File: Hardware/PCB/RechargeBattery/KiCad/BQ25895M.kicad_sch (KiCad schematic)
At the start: 19 parts, among them IC1 BQ25895MRTWT, J1 USB_C_Receptacle_USB2.0_16P

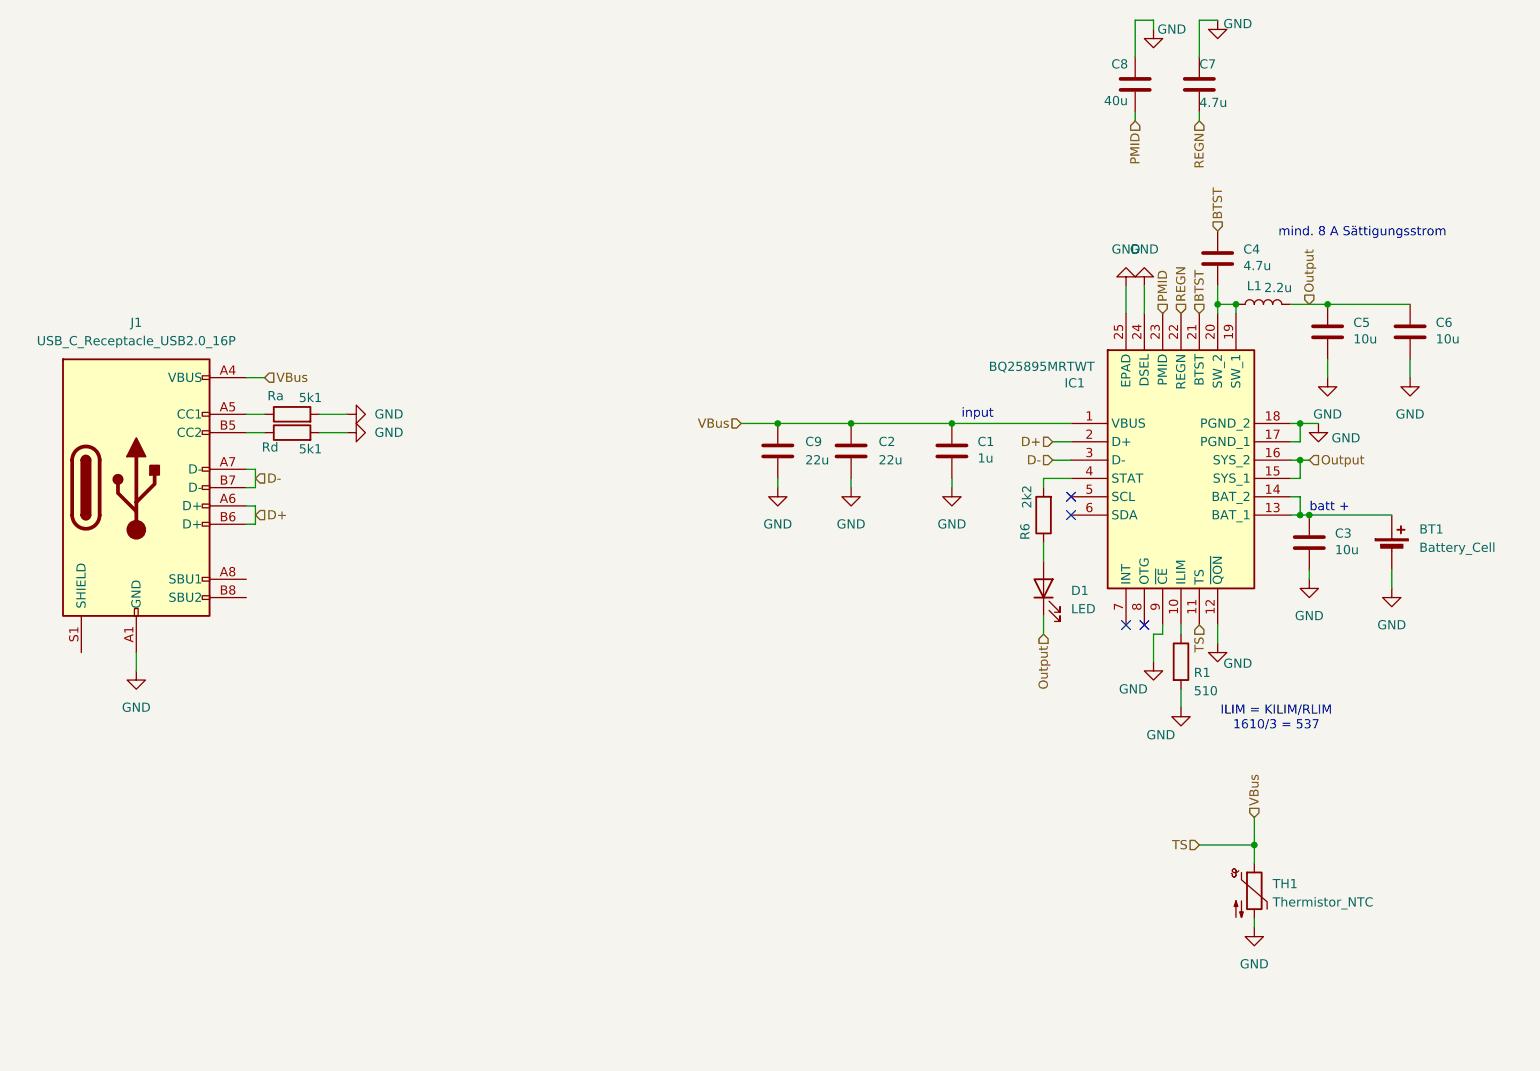
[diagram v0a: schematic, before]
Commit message: rechargeBatterie schematic finsished
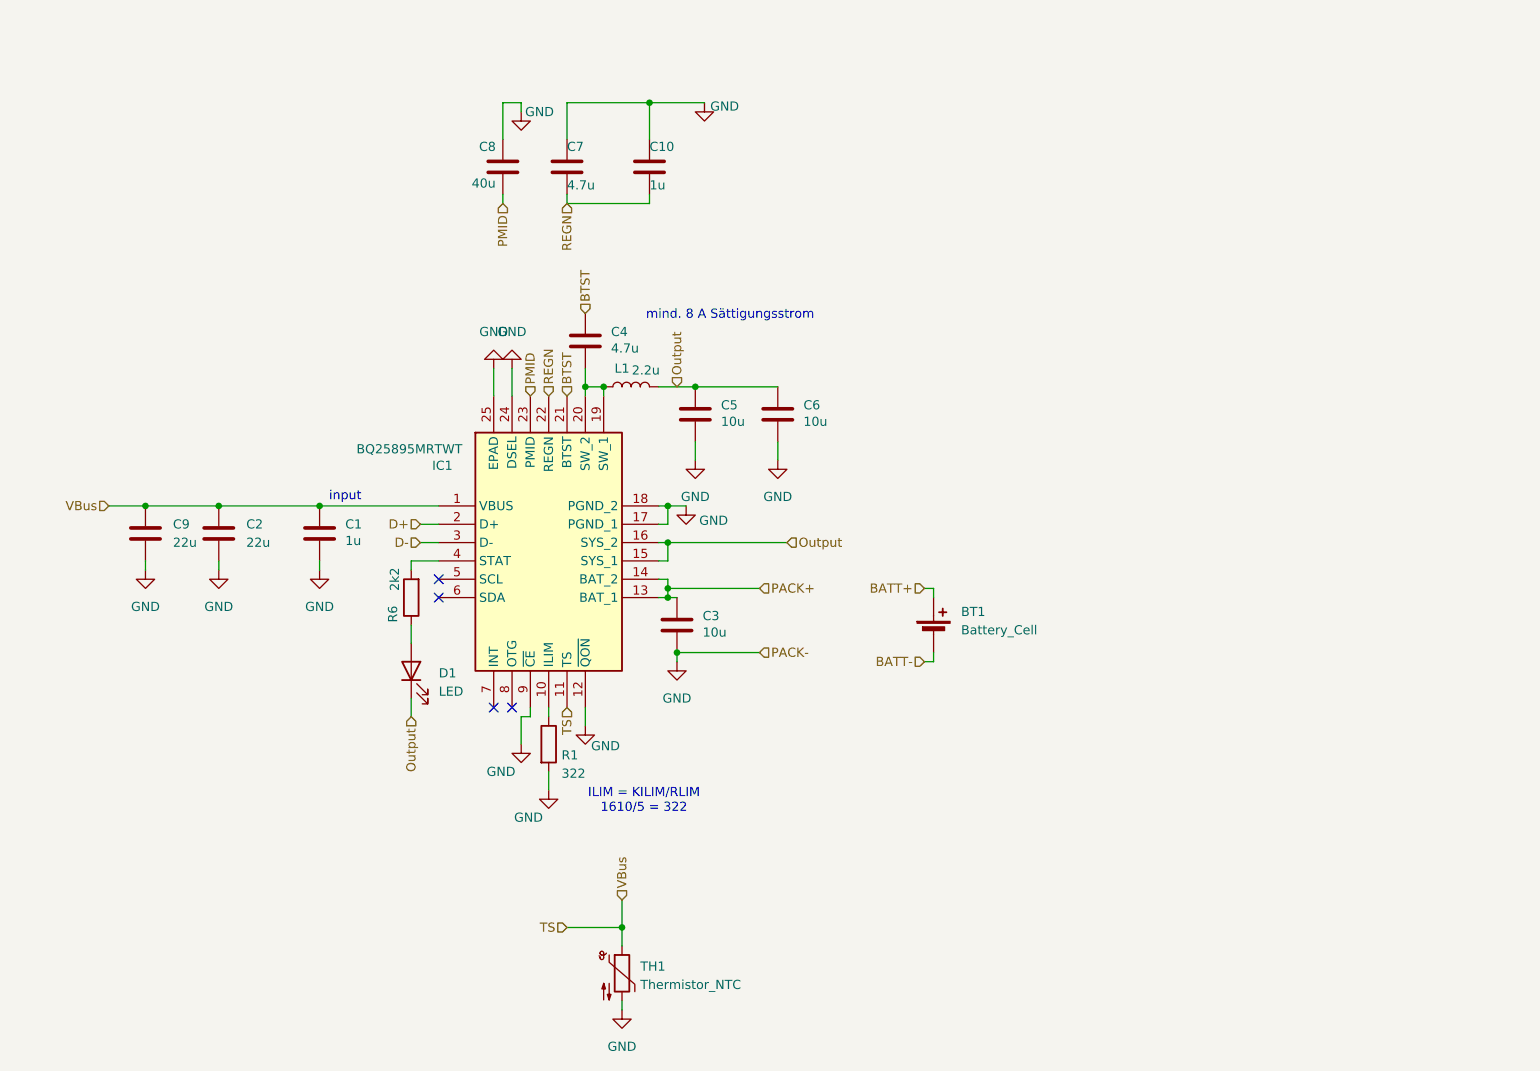
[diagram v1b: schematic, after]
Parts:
- removed J1: USB_C_Receptacle_USB2.0_16P, Connector_USB:USB_C_Receptacle_GCT_USB4085, symbol Connector:USB_C_Receptacle_USB2.0_16P
- removed Ra, Rd: 5k1, Resistor_SMD:R_0603_1608Metric, symbol Device:R
- added C10: 1u, Capacitor_SMD:C_0603_1608Metric, symbol Device:C
- D1: footprint (none) -> LED_SMD:LED_0603_1608Metric
- R1: value 510 -> 322
- TH1: footprint (none) -> Resistor_SMD:R_0603_1608Metric
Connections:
- net GND: now also C10.1; no longer BT1.2 (-)
- net REGN: now also C10.2
- net PACK+: now reaches C3.1, IC1.13 (BAT_1), IC1.14 (BAT_2)
- net PACK+: no longer BT1.1 (+)
- new net BATT+: BT1.1 (+)
- new net BATT-: BT1.2 (-)
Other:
- note added: "ILIM = KILIM/RLIM 1610/5 = 322"
- note removed: "ILIM = KILIM/RLIM 1610/3 = 537"
- note removed: "batt +"
- moved on the sheet: BT1, C1, C2, C3, C4, C5, C6, C7, C8, C9, D1, IC1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
